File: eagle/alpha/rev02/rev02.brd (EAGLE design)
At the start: 100 x 70 mm, 317 parts, among them CN1 HOST, IC3 N25Q128A13ES, Q1 25MHz, Q2 32768, Q3 2N7002, Q5 ASFL1, Q6 2N7002, T1 BC847, T2 BC847, T3 BC818, U1 LP3985IM5-3.3, U2 MC74HC1G14DTT1G, U3 ATTINY828R-AU, U4 MC14551BDG, U5 23K640-I/SN, U6 MCP79412-I/SN, U7 XC7A200TFBG484, Y1 12 MHz +- 30 ppm

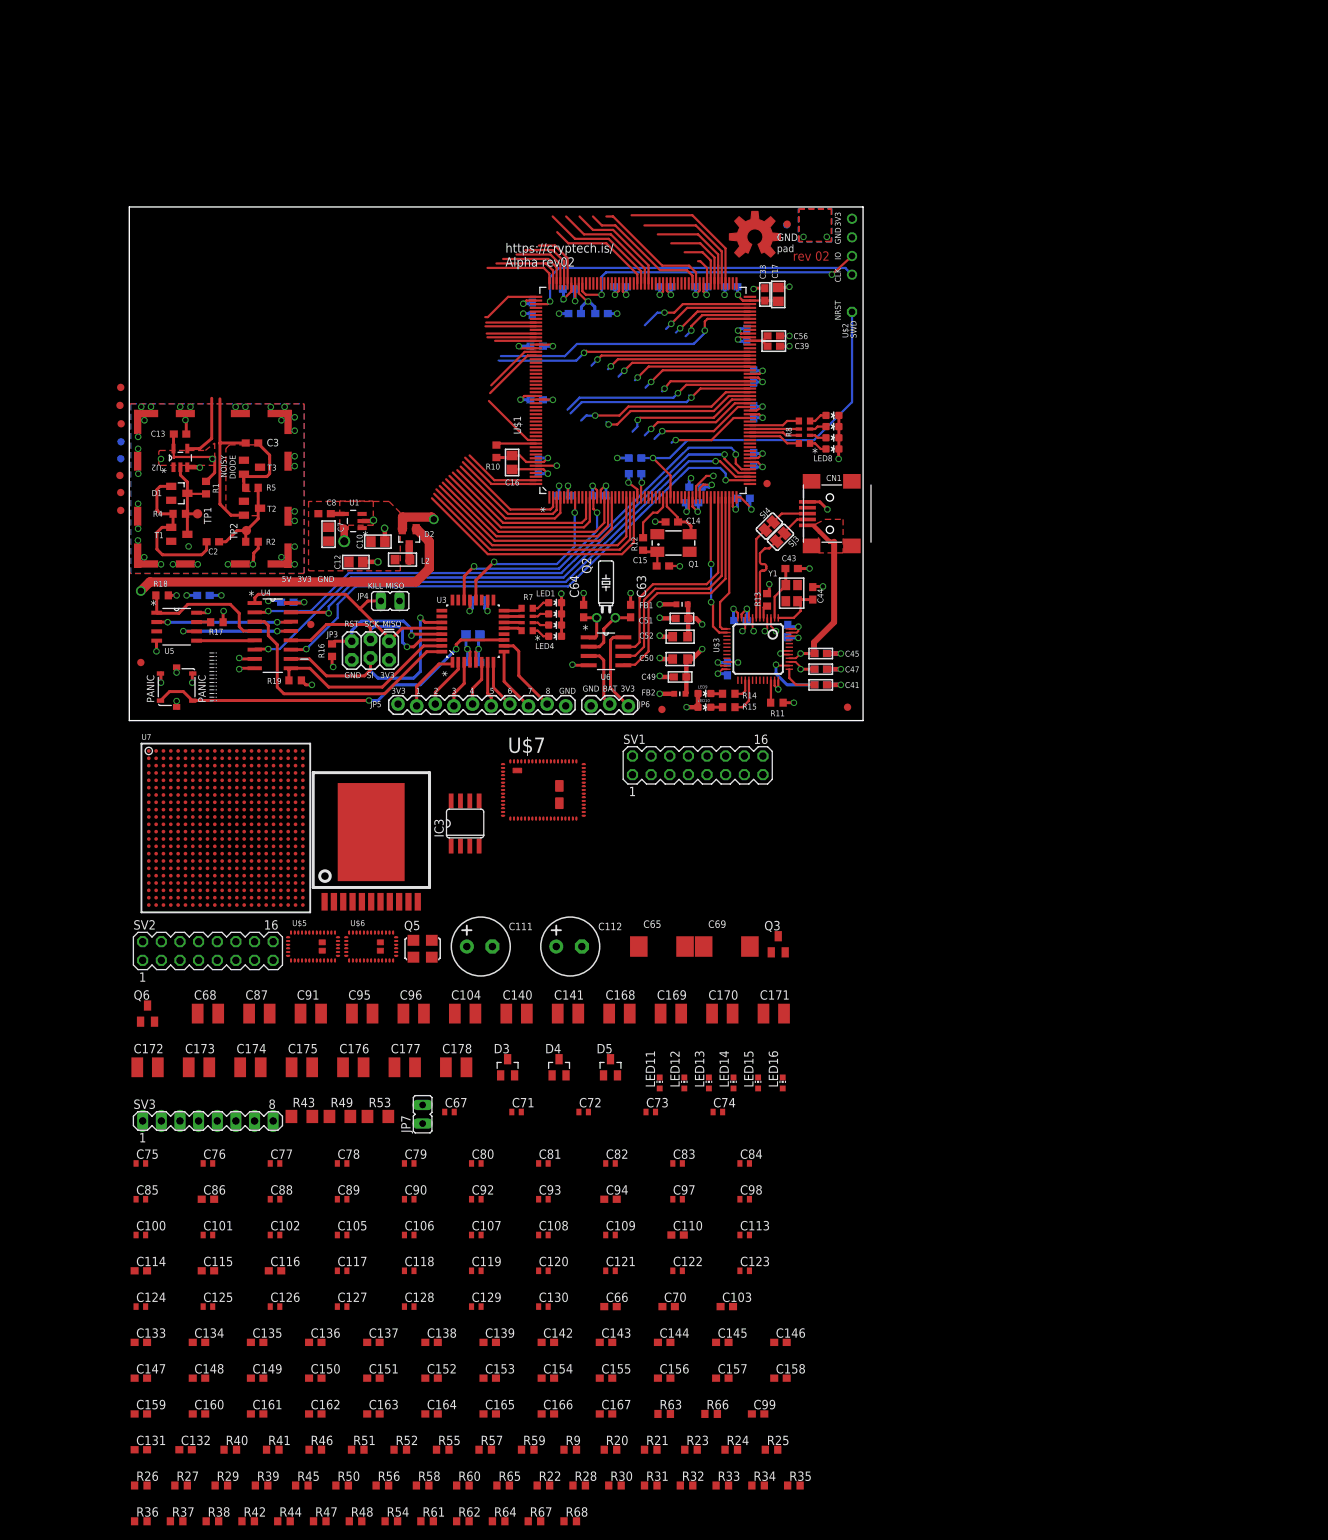
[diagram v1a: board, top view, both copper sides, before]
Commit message: fixed most of the FMC bus, grouped components.
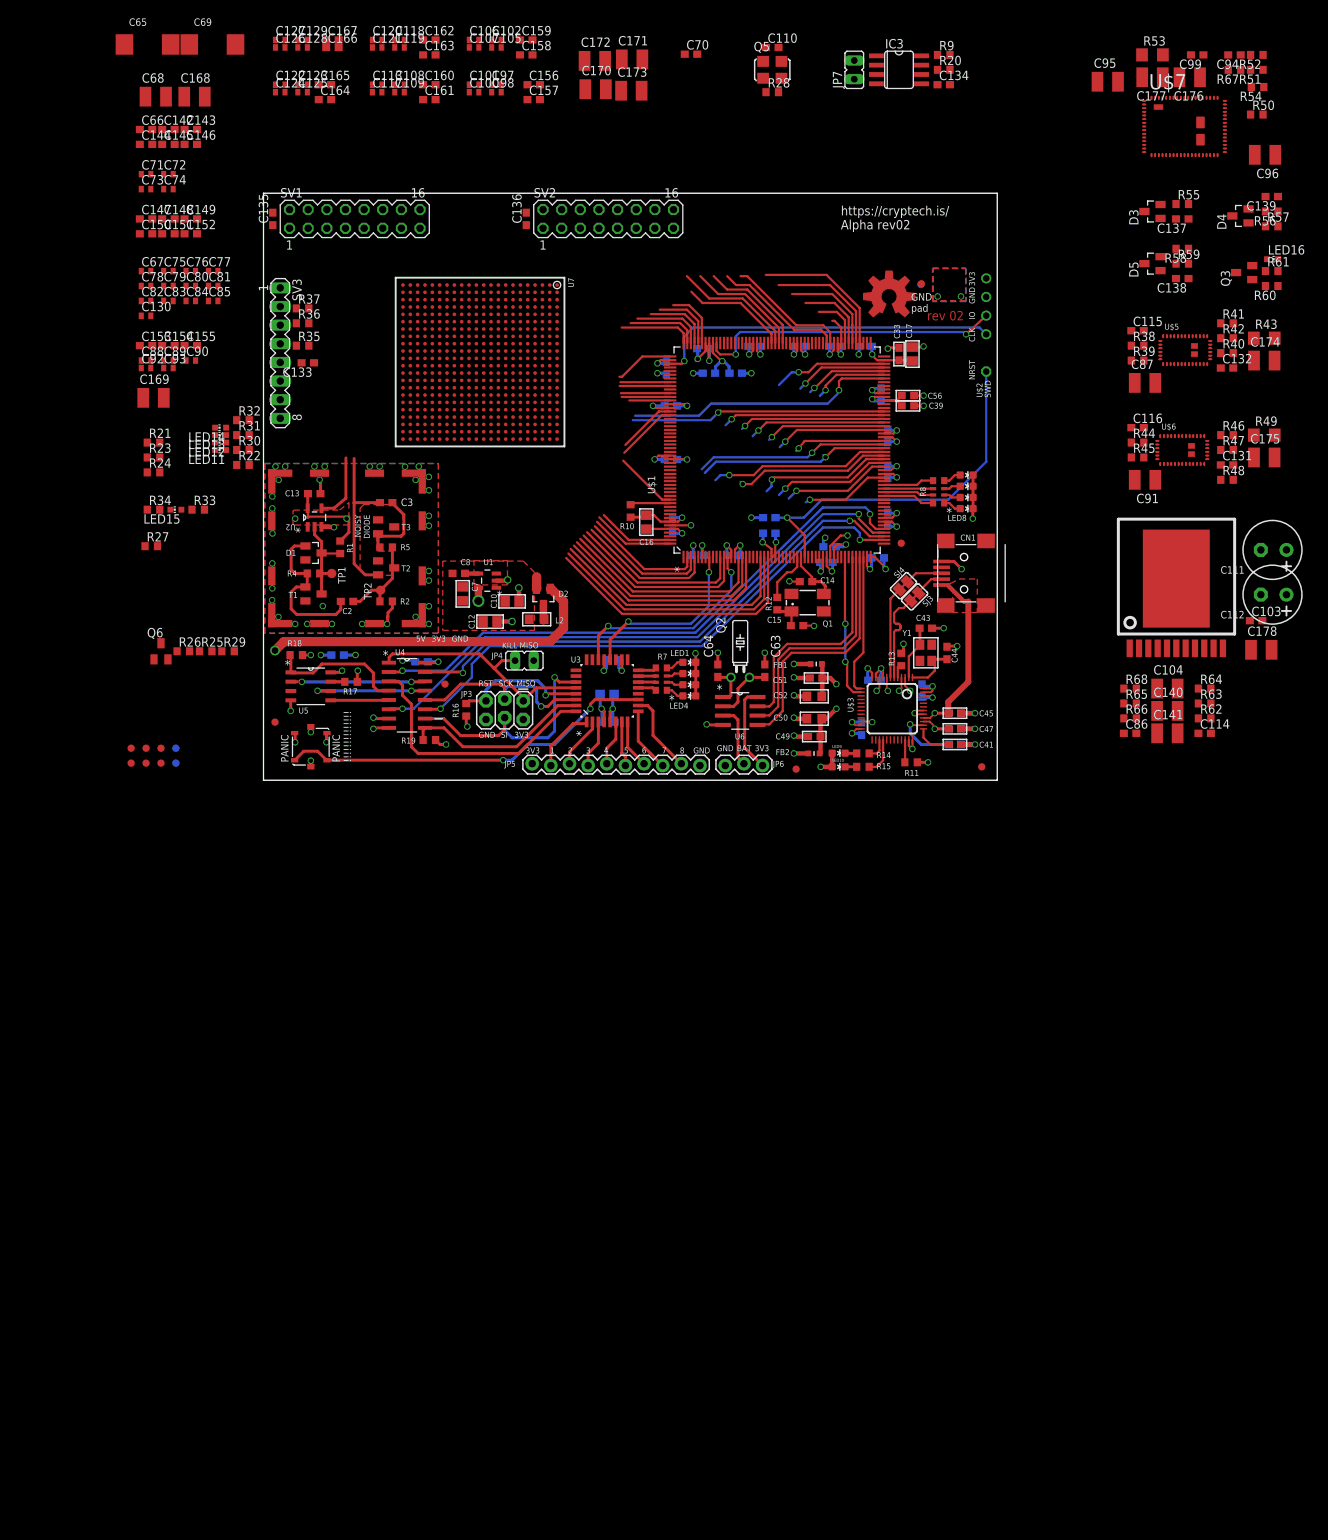
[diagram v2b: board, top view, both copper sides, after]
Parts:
- moved R54 228.4 mm to (155.5, 95.2), turned to 180 degrees
- moved R50 224.6 mm to (155.4, 91.4)
- moved R51 224.5 mm to (155.4, 97.5), turned to 180 degrees
- moved R52 223.1 mm to (155.4, 99.6), turned to 180 degrees
- moved R67 219.6 mm to (152.4, 97.5), turned to 180 degrees
- moved R56 211.8 mm to (157.5, 78.2), turned to 180 degrees
- moved R42 209.3 mm to (151.4, 61.0)
- moved R61 205.6 mm to (157.5, 70.1)
- moved C132 204.6 mm to (151.4, 56.9)
- moved R38 203.9 mm to (139.2, 59.9)
- moved R40 202.0 mm to (151.4, 58.9)
- moved R41 201.2 mm to (151.4, 63.0)
- moved C131 199.8 mm to (151.4, 43.7)
- moved C134 199.2 mm to (112.8, 95.5)
- moved R57 198.2 mm to (157.5, 76.2)
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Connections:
- net FPGA_FMC_A22 renamed FMC_A22
- net FPGA_FMC_A23 renamed FMC_A23
- net FPGA_FMC_A24 renamed FMC_A24
- net FPGA_FMC_A25 renamed FMC_A25
- removed net FPGA_FMC_A0: U7.Y17
- removed net FPGA_FMC_A1: U7.Y16
- removed net FPGA_FMC_A10: U7.AA14
- removed net FPGA_FMC_A11: U7.W14
- removed net FPGA_FMC_A12: U7.Y14
- removed net FPGA_FMC_A13: U7.AB11
- removed net FPGA_FMC_A14: U7.AB12
- removed net FPGA_FMC_A15: U7.AA9
- removed net FPGA_FMC_A16: U7.AB10
- removed net FPGA_FMC_A17: U7.AA10
- removed net FPGA_FMC_A18: U7.AA11
- removed net FPGA_FMC_A19: U7.V10
- removed net FPGA_FMC_A2: U7.AA16
- removed net FPGA_FMC_A20: U7.W10
- removed net FPGA_FMC_A21: U7.Y11
- removed net FPGA_FMC_A3: U7.AB16
- removed net FPGA_FMC_A4: U7.AB17
- removed net FPGA_FMC_A5: U7.AA13
- removed net FPGA_FMC_A6: U7.AB13
- removed net FPGA_FMC_A7: U7.AA15
- removed net FPGA_FMC_A8: U7.AB15
- removed net FPGA_FMC_A9: U7.Y13
- removed net FPGA_FMC_D0: U7.T3
- removed net FPGA_FMC_D1: U7.T1
- removed net FPGA_FMC_D10: U7.Y1
- removed net FPGA_FMC_D11: U7.U3
- removed net FPGA_FMC_D12: U7.V3
- removed net FPGA_FMC_D13: U7.AA1
- removed net FPGA_FMC_D14: U7.AB1
- removed net FPGA_FMC_D15: U7.AB3
- removed net FPGA_FMC_D16: U7.AB2
- removed net FPGA_FMC_D17: U7.Y3
- removed net FPGA_FMC_D18: U7.AA3
- removed net FPGA_FMC_D19: U7.AA5
- removed net FPGA_FMC_D2: U7.U1
- removed net FPGA_FMC_D20: U7.AB5
- removed net FPGA_FMC_D21: U7.Y4
- removed net FPGA_FMC_D22: U7.AA4
- removed net FPGA_FMC_D23: U7.V4
- removed net FPGA_FMC_D24: U7.W4
- removed net FPGA_FMC_D25: U7.R4
- removed net FPGA_FMC_D26: U7.T4
- removed net FPGA_FMC_D27: U7.T5
- removed net FPGA_FMC_D28: U7.U5
- removed net FPGA_FMC_D29: U7.W6
- removed net FPGA_FMC_D3: U7.U2
- removed net FPGA_FMC_D30: U7.W5
- removed net FPGA_FMC_D31: U7.U6
- removed net FPGA_FMC_D4: U7.V2
- removed net FPGA_FMC_D5: U7.R3
- removed net FPGA_FMC_D6: U7.R2
- removed net FPGA_FMC_D7: U7.W2
- removed net FPGA_FMC_D8: U7.Y2
- removed net FPGA_FMC_D9: U7.W1
- removed net FPGA_FMC_NE1: U7.V5
- removed net FPGA_FMC_NL: U7.R6
- removed net FPGA_FMC_NOE: U7.T6
- removed net FPGA_FMC_NWAIT: U7.Y6
- removed net FPGA_FMC_NWE: U7.AA6
- net FMC_A0: now also U7.Y17
- net FMC_A1: now also U7.Y16
- net FMC_A10: now also U7.AA14
- net FMC_A11: now also U7.W14
- net FMC_A12: now also U7.Y14
- net FMC_A13: now also U7.AB11
- net FMC_A14: now also U7.AB12
- net FMC_A15: now also U7.AA9
- net FMC_A16: now also U7.AB10
- net FMC_A17: now also U7.AA10
- net FMC_A18: now also U7.AA11
- net FMC_A19: now also U7.V10
- net FMC_A2: now also U7.AA16
- net FMC_A20: now also U7.W10
- net FMC_A21: now also U7.Y11
- net FMC_A3: now also U7.AB16
- net FMC_A4: now also U7.AB17
- net FMC_A5: now also U7.AA13
- net FMC_A6: now also U7.AB13
- net FMC_A7: now also U7.AA15
- net FMC_A8: now also U7.AB15
- net FMC_A9: now also U7.Y13
- net FMC_D0: now also U7.T3
- net FMC_D1: now also U7.T1
- net FMC_D10: now also U7.Y1
- net FMC_D11: now also U7.U3
- net FMC_D12: now also U7.V3
- net FMC_D13: now also U7.AA1
- net FMC_D14: now also U7.AB1
- net FMC_D15: now also U7.AB3
- net FMC_D16: now also U7.AB2
- net FMC_D17: now also U7.Y3
- net FMC_D18: now also U7.AA3
- net FMC_D19: now also U7.AA5
- net FMC_D2: now also U7.U1
- net FMC_D20: now also U7.AB5
- net FMC_D21: now also U7.Y4
- net FMC_D22: now also U7.AA4
- net FMC_D23: now also U7.V4
- net FMC_D24: now also U7.W4
- net FMC_D25: now also U7.R4
- net FMC_D26: now also U7.T4
- net FMC_D27: now also U7.T5
- net FMC_D28: now also U7.U5
- net FMC_D29: now also U7.W6
- net FMC_D3: now also U7.U2
- net FMC_D30: now also U7.W5
- net FMC_D31: now also U7.U6
- net FMC_D4: now also U7.V2
- net FMC_D5: now also U7.R3
- net FMC_D6: now also U7.R2
- net FMC_D7: now also U7.W2
- net FMC_D8: now also U7.Y2
- net FMC_D9: now also U7.W1
- net FMC_NE1: now also U7.V5
- net FMC_NL: now also U7.R6
- net FMC_NOE: now also U7.T6
- net FMC_NWAIT: now also U7.Y6
- net FMC_NWE: now also U7.AA6
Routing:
- net P-5.0V_MAIN: track 6.05 -> 1.66 mm, vias 1 -> 0
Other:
- board size 100 x 70 mm -> 100 x 80 mm

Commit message: more changes, end of today
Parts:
- removed D2: BAT54C, diode:SOT23
- removed L2: 10uH, microbuilder:_0805
- removed SJ3, SJ4: (no value), microbuilder:SOLDERJUMPER_CLOSEDWIRE
- added JP1: 5.5x2.1mm Barrel, SparkFun-Connectors:POWER_JACK_SMD
- C10, C7: value 1.0 uF X7R -> 1.0 uF
- C12: value 10 uF X7R 25v -> 10 uF
- C13, C2, C3: value 0.1µF -> 0.1 uF
- C16, C17, C50, C52: value 10 uF X7R 10v -> 10 uF
- C30: value 1 uF X7R 10v -> 1 uF
- C41, C42, C46, C48, C49, C51: value 0.1 uF X7R 10v -> 0.1 uF
- C45, C47: value 4.7 uF X7R 10v -> 4.7 uF
- C8: value 10NF C0G -> 10NF
- LED15: value (none) -> R
- R13: value 12K 1% -> 12K
- Y1: value 12 MHz +- 30 ppm -> 12 MHz
- moved LED16 33.8 mm to (134.2, 47.3)
- moved Q3 33.8 mm to (130.4, 45.5)
- moved R60 33.8 mm to (134.1, 43.7)
- moved R61 33.8 mm to (134.1, 45.7)
- moved R59 16.5 mm to (134.1, 58.9)
- moved R58 16.5 mm to (134.1, 61.0)
- moved C138 16.5 mm to (134.1, 56.9)
- moved D5 16.5 mm to (130.0, 58.9)
- moved Q6 8.19 mm to (5.08, 26.4)
- moved R25 8.19 mm to (11.2, 26.4)
- moved R26 8.19 mm to (8.13, 26.4)
- moved R29 8.19 mm to (14.2, 26.4)
- moved C87 1.02 mm to (140.2, 55.9)
- moved R40 1.02 mm to (151.4, 59.9)
- moved C115 1.02 mm to (139.2, 63.0)
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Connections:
- removed net 5V: C10.1, C12.1, L2.2, U1.1, U1.3
- removed net FPGA_MKM_CS_N: U7.T21
- removed net FPGA_MKM_MISO: U7.R19
- removed net FPGA_MKM_MOSI: U7.P19
- removed net FPGA_MKM_SCLK: U7.U21
- removed net MINUS15V_STABLE: C3.1, T2.2
- removed net N$14: D2.3, L2.1
- removed net P-5.0V_MAIN: D2.2
- removed net USBDM: CN1.D-, SJ3.1
- removed net USBDP: CN1.D+, SJ4.1
- removed net USB_PWR_VBUS: D2.1
- new net 15V_STABLE: R2.1
- net AGND: no longer R2.1
- net FPGA_DONE: now also U$1.36
- net GND: now also C3.1, JP1.P$4, T2.2
- net MKM_FPGA_CS: now also U7.T21; no longer U$1.57
- net MKM_FPGA_MISO: now also U7.R19; no longer U$1.55
- net MKM_FPGA_MOSI: now also U7.P19; no longer U$1.56
- net MKM_FPGA_SCK: now also U7.U21; no longer U$1.54
- net PWR_18V: now also JP1.VIN0
- net USB_DM: now also CN1.D-; no longer SJ3.2
- net USB_DP: now also CN1.D+; no longer SJ4.2
- net VCC_5V0: now also C10.1, C12.1, U1.1, U1.3
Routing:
- net MKM_FPGA_CS: track 78.8 -> 15.0 mm, vias 2 -> 1
- net MKM_FPGA_MOSI: track 79.8 -> 17.2 mm, vias 2 -> 1
- net MKM_FPGA_MISO: track 72.5 -> 10.9 mm, vias 2 -> 1
- net MKM_FPGA_SCK: track 75.5 -> 13.9 mm, vias 2 -> 1
- net USB_PWR_VBUS: track 46.7 -> 0.00 mm, vias 1 -> 0
- net MINUS15V_STABLE: track 21.8 -> 0.00 mm
- net USBDP: track 5.14 -> 0.00 mm
- net USBDM: track 4.62 -> 0.00 mm
- net AGND: track 9.52 -> 5.14 mm, vias 34 -> 33
- net USB_DM: track 12.8 -> 15.6 mm
- net N$14: track 2.38 -> 0.00 mm
- net USB_DP: track 12.5 -> 14.2 mm
- net P-5.0V_MAIN: track 1.66 -> 0.00 mm
- added copper zone on layer 1, net VCC_5V0
- removed copper zone on layer 1, net 5V

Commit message: fix some errata
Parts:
- removed Q1: 25MHz, adafruit:CTS406
- removed Q2: 32768, crystal:TC26H
- removed R22, R30, R31, R32: 330, resistor:R0603
- added Q4: (no value), adafruit:NX3225
- added R3: 330R, Panasonic-EXB-ERJ:RESCAXE80P320X160X60-8N
- added X1: (no value), adafruit:XTAL3215
- C14, C15: value 10 pF -> 5 pF
- C25, C28, C29, C53, C54, C55: value 0.1uF -> 0.1 uF
- moved C15 4.32 mm to (90.4, 25.4), turned to 270 degrees
- moved R12 3.82 mm to (91.2, 28.4), turned to 180 degrees
- moved C14 3.47 mm to (96.5, 25.4), turned to 90 degrees
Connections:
- net AVR_PANIC: no longer U$4.A1
- net FPGA_GPIO_LED_0: now also R3.4; no longer R22.2
- net FPGA_GPIO_LED_1: now also R3.3; no longer R30.2
- net FPGA_GPIO_LED_2: now also R3.2; no longer R31.2
- net FPGA_GPIO_LED_3: now also R3.1; no longer R32.2
- net GND: now also Q4.2, Q4.4
- net N$21: now also Q4.1; no longer Q1.1
- net N$27: now also R3.5; no longer R22.1
- net N$28: now also R3.6; no longer R30.1
- net N$29: now also R3.7; no longer R31.1
- net N$30: now also R3.8; no longer R32.1
- net OSC_OUT: now also Q4.3; no longer Q1.3
- net RTC_X1: now also X1.P$1; no longer Q2.1
- net RTC_X2: now also X1.P$2; no longer Q2.2
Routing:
- net USB_DM: track 15.6 -> 6.14 mm
- net RTC_X2: track 8.46 -> 0.13 mm
- net USB_DP: track 14.2 -> 6.68 mm
- net OSC_OUT: track 8.12 -> 1.22 mm
- net OSC_IN: track 6.98 -> 1.32 mm
- net AVR_PANIC: track 51.6 -> 46.3 mm
- net RTC_X1: track 5.52 -> 0.96 mm
- net N$21: track 3.98 -> 0.00 mm
- net GND: track 172.4 -> 169.5 mm, vias 65 -> 64
